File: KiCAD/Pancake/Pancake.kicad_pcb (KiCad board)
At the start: 2 copper layers, 170 parts, among them IC10 LF347N, IC3 LF347N, IC4 LF347N, IC5 LF347N, IC6 LF347N, IC7 LF347N, IC8 LF347N, IC9 LF347N, J1 Conn_01x08_Male, J2 Conn_01x08_Male, J3 Conn_01x08_Male, J4 Conn_01x10_Male, J5 Conn_01x08_Male, J6 Conn_01x08_Male

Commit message: Ribbon cable connector, arduino layout
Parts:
- added J7: Conn_02x15_Top_Bottom, Connector_PinSocket_2.54mm:PinSocket_2x15_P2.54mm_Vertical, F.Cu at (134.6, 78.7)
- J1, J2, J3, J4, J5, J6: moved to B.Cu
- moved J1 17.3 mm to (22.1, 36.5)
- moved J2 17.3 mm to (26.8, 36.5)
- moved J3 17.3 mm to (31.4, 36.5)
- moved J4 17.3 mm to (17.5, 36.5)
- moved J5 17.3 mm to (36.1, 36.5)
- moved J6 17.3 mm to (40.7, 36.5)

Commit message: Arduino laid out
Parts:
- removed J6: Conn_01x08_Male, Connector_PinHeader_2.54mm:PinHeader_1x08_P2.54mm_Vertical
- added J101: TB001-500-04BE, SamacSys_Parts:TB00150004BE, F.Cu at (-177.7, 81.0)
- added J102: TB001-500-03BE, SamacSys_Parts:TB00150003BE, F.Cu at (-182.2, 132.0)
- added Q901: ULN2003AIN, SamacSys_Parts:DIP794W53P254L1930H508Q16N, F.Cu at (-117.2, 43.0)
- added Q902: ULN2003AIN, SamacSys_Parts:DIP794W53P254L1930H508Q16N, F.Cu at (-95.1, 24.4)
- added R101: PWR220T-35-8R00F, SamacSys_Parts:TO508P438X1010X1539-2P, F.Cu at (-182.0, 140.6)
- added R901: 50K, Resistor_THT:R_Axial_DIN0207_L6.3mm_D2.5mm_P10.16mm_Horizontal, F.Cu at (-107.8, 49.2)
- added R902: 50K, Resistor_THT:R_Axial_DIN0207_L6.3mm_D2.5mm_P10.16mm_Horizontal, F.Cu at (-110.1, 45.1)
- added R903: 50K, Resistor_THT:R_Axial_DIN0207_L6.3mm_D2.5mm_P10.16mm_Horizontal, F.Cu at (-121.1, 59.7)
- added R904: 50K, Resistor_THT:R_Axial_DIN0207_L6.3mm_D2.5mm_P10.16mm_Horizontal, F.Cu at (-110.1, 41.1)
- added R905: 50K, Resistor_THT:R_Axial_DIN0207_L6.3mm_D2.5mm_P10.16mm_Horizontal, F.Cu at (-110.1, 37.0)
- added R906: 50K, Resistor_THT:R_Axial_DIN0207_L6.3mm_D2.5mm_P10.16mm_Horizontal, F.Cu at (-121.1, 55.6)
- added RelayA901: 833H-1A-F-S-12VDC, SamacSys_Parts:833H1AFS12VDC, F.Cu at (-185.9, 41.7)
- added RelayB901: 833H-1A-F-S-12VDC, SamacSys_Parts:833H1AFS12VDC, F.Cu at (-163.8, 23.1)
- added RelayC901: 833H-1A-F-S-12VDC, SamacSys_Parts:833H1AFS12VDC, F.Cu at (-185.9, 60.3)
- added RelayD901: 833H-1A-F-S-12VDC, SamacSys_Parts:833H1AFS12VDC, F.Cu at (-163.8, 41.7)
- added RelayE901: 833H-1A-F-S-12VDC, SamacSys_Parts:833H1AFS12VDC, F.Cu at (-141.7, 23.1)
- added RelayF901: 833H-1A-F-S-12VDC, SamacSys_Parts:833H1AFS12VDC, F.Cu at (-163.8, 60.3)
- added RelayG901: 833H-1A-F-S-12VDC, SamacSys_Parts:833H1AFS12VDC, F.Cu at (-141.7, 41.7)
- added RelayH901: 833H-1A-F-S-12VDC, SamacSys_Parts:833H1AFS12VDC, F.Cu at (-141.7, 60.3)
- added RelayI901: 833H-1A-F-S-12VDC, SamacSys_Parts:833H1AFS12VDC, F.Cu at (-185.9, 23.1)
- added RelayJ901: 833H-1A-F-S-12VDC, SamacSys_Parts:833H1AFS12VDC, F.Cu at (-119.6, 23.1)
- J4: value Conn_01x10_Male -> Conn_01x08_Male; footprint Connector_PinHeader_2.54mm:PinHeader_1x10_P2.54mm_Vertical -> Connector_PinHeader_2.54mm:PinHeader_1x08_P2.54mm_Vertical
- moved J7 318.7 mm to (-184.1, 76.8)
- moved R18 249.1 mm to (-174.1, 113.4)
- moved R12 245.3 mm to (-157.6, 107.0)
- moved R27 245.3 mm to (-157.6, 111.1)
- moved C6 241.2 mm to (-174.2, 117.0)
- moved R7 233.0 mm to (-147.4, 115.1)
- moved R11 230.9 mm to (-146.6, 103.0)
- moved IC3 228.9 mm to (-167.0, 97.0)
- moved R25 224.2 mm to (-187.4, 116.7)
- moved C39 223.6 mm to (-92.8, 91.5)
- moved R76 222.4 mm to (-58.5, 92.3)
- moved R56 221.3 mm to (-95.0, 79.8)
- moved C37 220.4 mm to (-84.8, 91.5)
- moved R73 220.0 mm to (-47.5, 75.6)
- moved R75 220.0 mm to (-47.5, 71.6)
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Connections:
- net /D0 renamed Net-(J5-Pad8)
- net /D1 renamed Net-(J5-Pad7)
- C5 pad 2: /DAC0 -> /GuitarIn
- C6 pad 2: /DAC1 -> /AuxIn
- J1 pad 8: VDD -> +12V
- J2 pad 1: /A0 -> /ADC0
- J2 pad 2: /A1 -> /ADC1
- J2 pad 3: /A2 -> /ADC2
- J2 pad 4: /A3 -> /ADC3
- J2 pad 5: /A4 -> /ADC4
- J2 pad 6: /A5 -> /ADC5
- J2 pad 7: /A6 -> /ADC6
- J2 pad 8: /A7 -> /ADC7
- J3 pad 1: /A8 -> /ADC8
- J3 pad 2: /A9 -> /ADC9
- J3 pad 3: /A10 -> /ADC10
- J3 pad 4: /A11 -> /ADC11
- J4 pad 2: Net-(J4-Pad2) -> GND
- J4 pad 4: GND -> Net-(J4-Pad4)
- J4 pad 5: /D13 -> /D11
- J4 pad 6: /D12 -> /D10
- J4 pad 7: /D11 -> /D9
- J4 pad 8: /D10 -> /D8
- J7 pad 1: Net-(J7-Pad1) -> /GuitarIn
- J7 pad 10: Net-(J7-Pad10) -> /6VOut
- J7 pad 11: Net-(J7-Pad11) -> /NegDriverOut
- J7 pad 12: Net-(J7-Pad12) -> /PosDriverOut
- J7 pad 16: Net-(J7-Pad16) -> /DriveCCW
- J7 pad 17: Net-(J7-Pad17) -> /DriveMid
- J7 pad 18: Net-(J7-Pad18) -> /DriveCW
- J7 pad 19: Net-(J7-Pad19) -> /ToneCCW
- J7 pad 2: Net-(J7-Pad2) -> /AuxIn
- J7 pad 20: Net-(J7-Pad20) -> /ToneMid
- J7 pad 21: Net-(J7-Pad21) -> /ToneCW
- J7 pad 22: Net-(J7-Pad22) -> /VolumeCCW
- J7 pad 23: Net-(J7-Pad23) -> /VolumeMid
- J7 pad 24: Net-(J7-Pad24) -> /VolumeCW
- J7 pad 25: Net-(J7-Pad25) -> /PresenceIn
- J7 pad 26: Net-(J7-Pad26) -> /PresenceOut
- J7 pad 3: Net-(J7-Pad3) -> /PreampOut
- J7 pad 4: Net-(J7-Pad4) -> /GainStageOut
- J7 pad 5: Net-(J7-Pad5) -> /EmitterBypassOut
- J7 pad 6: Net-(J7-Pad6) -> /EmitterFollowerOut
- J7 pad 7: Net-(J7-Pad7) -> /SourceFollowerOut
- J7 pad 8: Net-(J7-Pad8) -> /12VOut
- J7 pad 9: Net-(J7-Pad9) -> /8VOut
- R1 pad 2: /PosDriverOut -> /DAC2
- R17 pad 2: /6VOut -> /EmitterFollowerOut
- R2 pad 2: /NegDriverOut -> /DAC1
- R21 pad 2: /SPRKNeg -> /SPRKPos
- R6 pad 2: /EmitterFollowerOut -> /6VOut

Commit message: Models
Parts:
- C10, C11, C12, C13, C14, C15, C16, C17, C18, C19, C20, C21, C22, C23, C24, C25, C26, C27, C28, C29, C30, C31, C32, C33, C34, C35, C36, C37, C38, C39, C40, C41, C42, C43, C44, C45, C46, C47, C48, C49, C5, C50, C51, C52, C53, C54, C55, C56, C57, C58, C59, C6, C60, C61, C62, C63, C64, C65, C66, C67, C68, C69, C7, C70, C71, C72, C73, C74, C75, C76, C8, C9: footprint Resistor_THT:R_Axial_DIN0204_L3.6mm_D1.6mm_P5.08mm_Horizontal -> Capacitor_THT:C_Disc_D4.3mm_W1.9mm_P5.00mm
- moved C6 1.14 mm to (-174.0, 118.1)

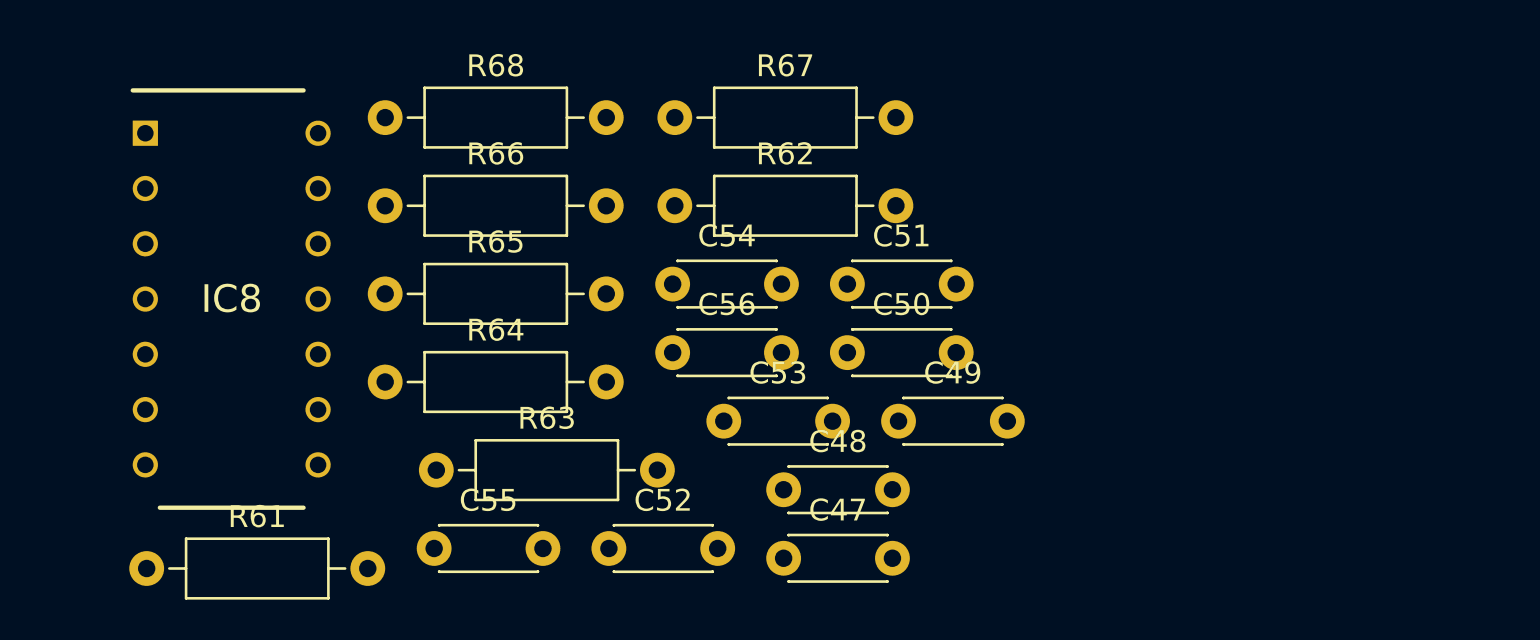
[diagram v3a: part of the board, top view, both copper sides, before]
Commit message: Moved giant component over
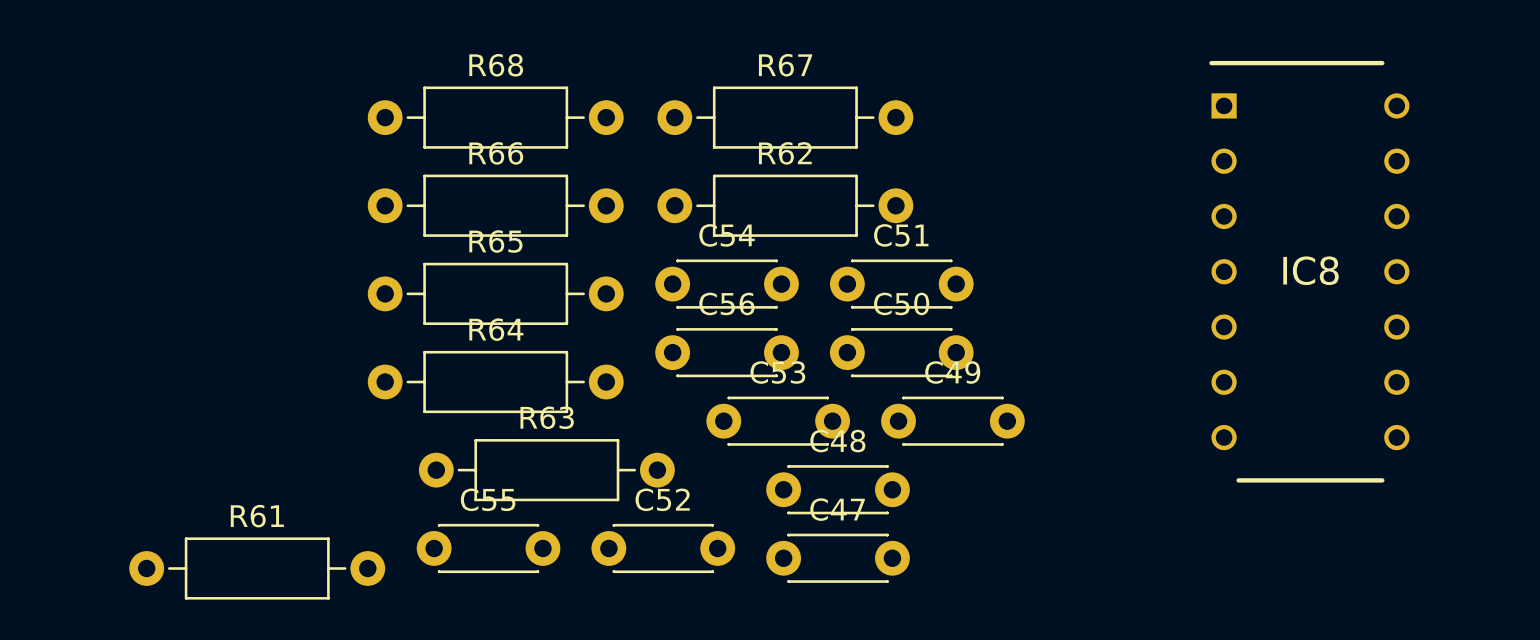
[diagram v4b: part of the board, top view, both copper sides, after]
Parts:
- moved IC8 49.6 mm to (19.1, 22.9)

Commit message: Have a few more filters to align but I believe the current layout can allow us to route.
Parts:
- moved R60 243.5 mm to (136.1, 67.1)
- moved C39 242.2 mm to (149.4, 98.6)
- moved R55 242.2 mm to (146.3, 96.5), turned to 180 degrees
- moved R57 241.3 mm to (146.3, 81.8), turned to 180 degrees
- moved R58 239.5 mm to (146.3, 72.1), turned to 180 degrees
- moved C40 237.6 mm to (154.4, 108.2), turned to 180 degrees
- moved C42 237.5 mm to (154.4, 103.6), turned to 180 degrees
- moved C37 235.1 mm to (149.4, 113.3)
- moved R53 233.0 mm to (136.1, 101.1)
- moved C45 231.9 mm to (154.4, 70.6), turned to 180 degrees
- moved R56 231.3 mm to (136.1, 86.4)
- moved IC7 231.1 mm to (129.1, 78.0)
- moved C38 229.0 mm to (149.4, 94.0)
- moved R54 228.9 mm to (146.3, 91.4), turned to 180 degrees
- moved C44 226.7 mm to (149.4, 75.2)
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
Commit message: Going to get big like Justin. Need to clean up ribbon,as there are a few resistors that run a long ways until their only connection.
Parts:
- moved R101 459.1 mm to (263.7, 30.5), turned to 180 degrees
- moved R18 445.0 mm to (269.7, 80.8), turned to 180 degrees
- moved R24 442.4 mm to (269.7, 70.6), turned to 180 degrees
- moved J7 439.7 mm to (255.5, 69.1)
- moved J102 433.0 mm to (238.8, 30.5)
- moved R20 431.5 mm to (269.7, 85.9), turned to 180 degrees
- moved R27 420.3 mm to (259.6, 60.5)
- moved R7 417.9 mm to (269.7, 91.4), turned to 180 degrees
- moved R22 413.2 mm to (269.7, 65.5), turned to 180 degrees
- moved J101 409.6 mm to (228.6, 29.5), turned to 180 degrees
- moved R10 408.8 mm to (247.9, 70.6), turned to 180 degrees
- moved R8 400.8 mm to (269.7, 108.7), turned to 180 degrees
- moved RelayI901 400.6 mm to (203.2, 118.4)
- moved R14 400.2 mm to (269.7, 102.6), turned to 180 degrees
- moved R28 399.8 mm to (269.7, 75.7), turned to 180 degrees
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
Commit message: Latest revision
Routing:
- net GND: track 0.00 -> 740.3 mm
- net +12V: track 0.00 -> 513.6 mm
- net /ADC1011/IN1: track 0.00 -> 321.8 mm
- net -12V: track 0.00 -> 311.8 mm
- net /ADC89/IN2: track 0.00 -> 246.2 mm
- net /ADC1011/IN2: track 0.00 -> 244.4 mm
- net /ADC89/IN1: track 0.00 -> 234.5 mm
- net /ADC67/IN2: track 0.00 -> 222.5 mm
- net /ADC01/IN2: track 0.00 -> 215.5 mm
- net /DriveMid: track 0.00 -> 215.4 mm
- net /ADC45/IN2: track 0.00 -> 215.1 mm
- net /ADC45/IN1: track 0.00 -> 190.0 mm
- net /ADC01/IN1: track 0.00 -> 185.0 mm
- net /ToneMid: track 0.00 -> 178.8 mm
- net /AuxIn: track 0.00 -> 170.3 mm
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
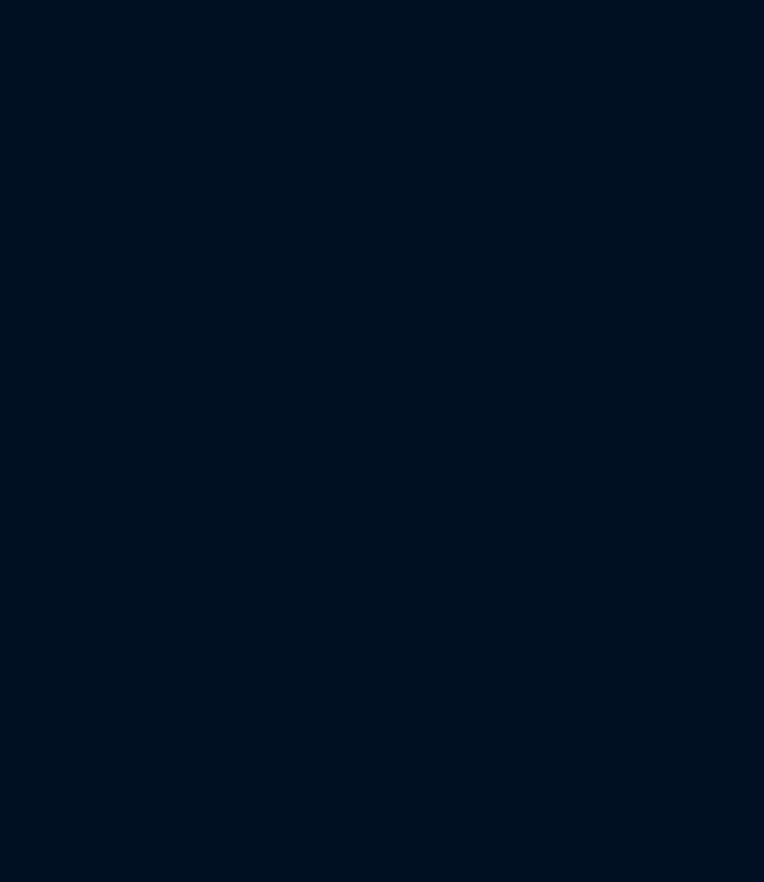
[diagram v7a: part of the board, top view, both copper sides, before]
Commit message: Lib updates and capacitor add. Simulation on power resistor working
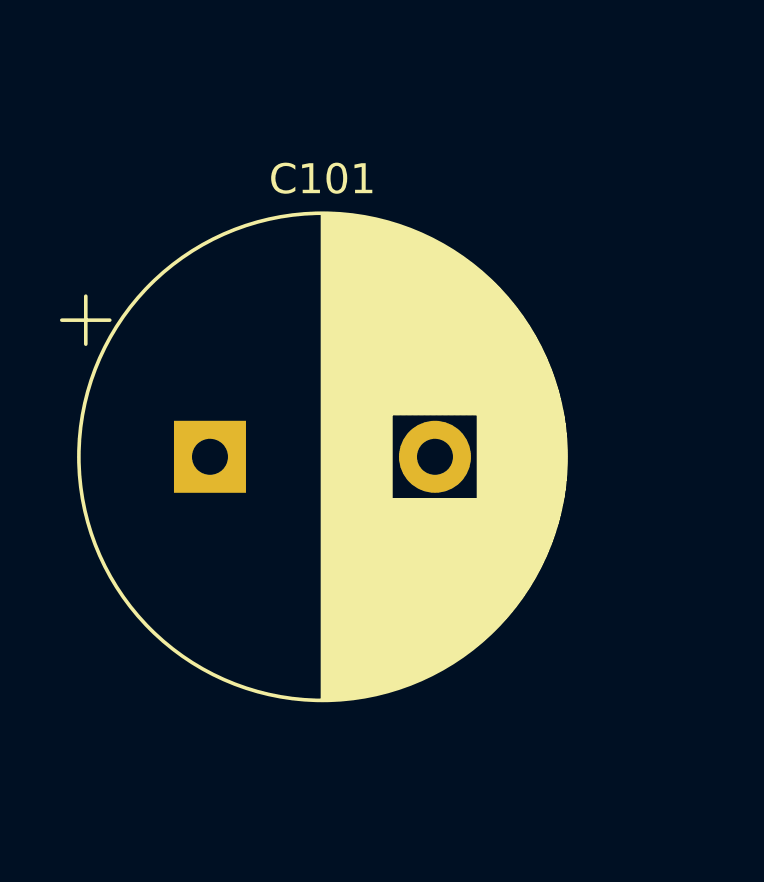
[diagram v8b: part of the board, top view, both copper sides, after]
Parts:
- added C101: 220nF, Capacitor_THT:CP_Radial_D16.0mm_P7.50mm, F.Cu at (27.9, 30.5)
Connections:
- R101 pad 2: /SPRKPos -> Net-(C101-Pad2)
